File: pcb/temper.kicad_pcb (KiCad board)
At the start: 2 copper layers, 111.3 x 90 mm, 48 parts, among them J2 nice_view, SW1 SW_PUSH, SW10 SW_PUSH, SW11 SW_PUSH, SW12 SW_PUSH, SW13 SW_PUSH, SW14 SW_PUSH, SW15 SW_PUSH, SW16 SW_PUSH, SW17 SW_PUSH, SW18 SW_PUSH, SW2 SW_PUSH, SW3 SW_PUSH, SW4 SW_PUSH, SW5 SW_PUSH, SW6 SW_PUSH, SW7 SW_PUSH, SW8 SW_PUSH, SW9 SW_PUSH, U1 nice_nano

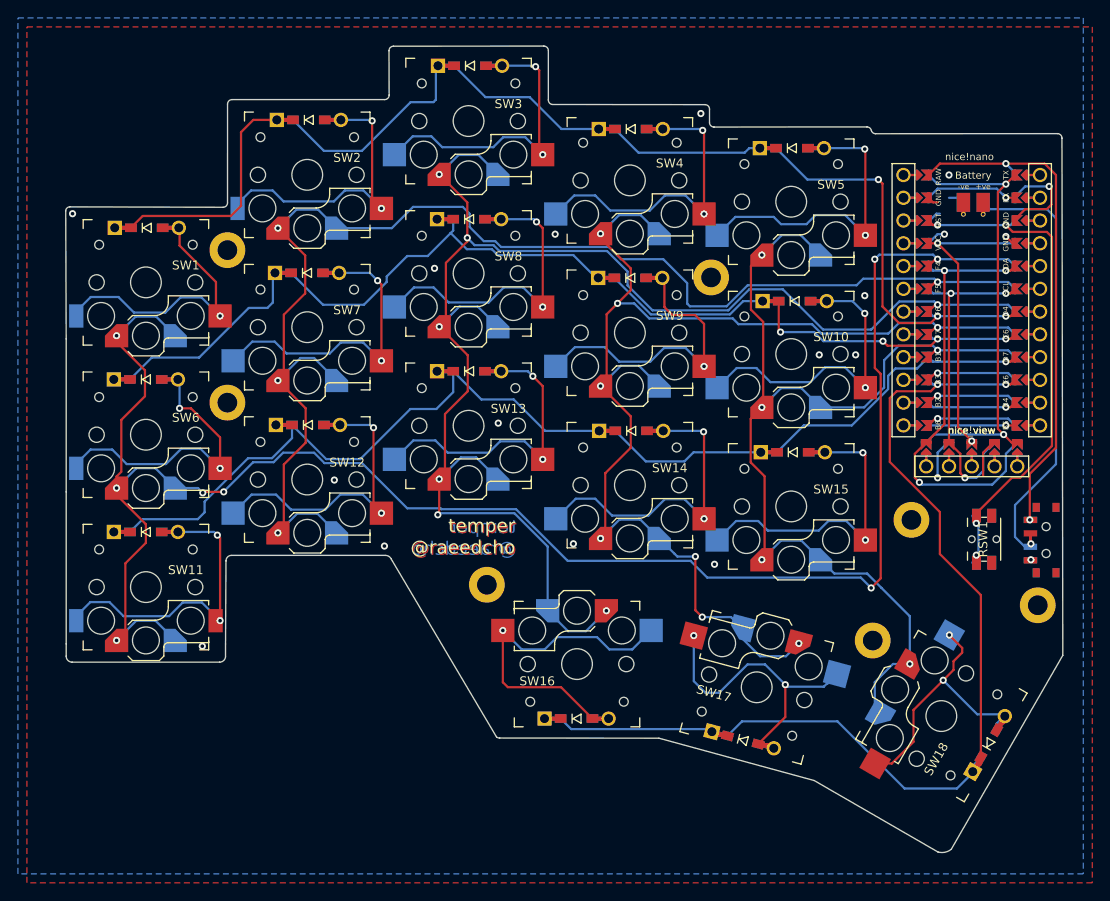
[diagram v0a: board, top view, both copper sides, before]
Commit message: Convert switches to Choc v2 sockets
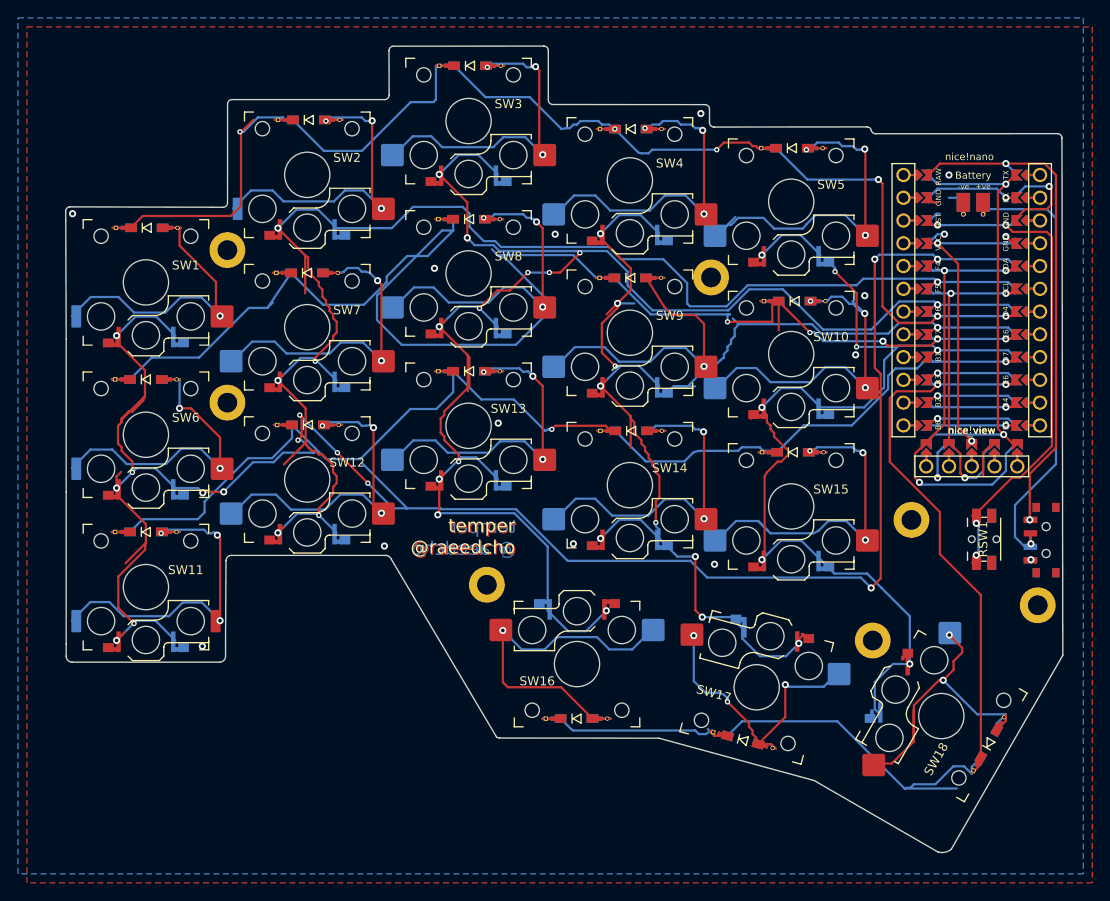
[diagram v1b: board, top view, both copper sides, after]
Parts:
- SW1, SW10, SW11, SW12, SW13, SW14, SW15, SW16, SW17, SW18, SW2, SW3, SW4, SW5, SW6, SW7, SW8, SW9: footprint dumta:Kailh_socket_PG1350_reversible -> dumta:Kailh_socket_Choc_V2_reversible
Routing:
- net row1: track 136.8 -> 186.3 mm, vias 4 -> 5
- net col0: track 205.5 -> 230.6 mm, vias 8 -> 14
- net col2: track 169.4 -> 187.2 mm, vias 7 -> 12
- net col3: track 138.5 -> 148.6 mm, vias 8 -> 10
- net col1: track 150.9 -> 159.6 mm, vias 4 -> 6
- net row3: track 122.1 -> 129.2 mm
- net Net-(D5-A): track 37.2 -> 43.6 mm, vias 2 -> 3
- net row0: track 150.3 -> 156.2 mm, vias 3 -> 6
- net row2: track 138.8 -> 143.7 mm, vias 1 -> 2
- net Net-(D15-A): track 37.2 -> 41.3 mm, vias 2 -> 3
- net Net-(D18-A): track 33.0 -> 36.8 mm
- net Net-(D4-A): track 37.4 -> 40.5 mm, vias 2 -> 3
- net Net-(D8-A): track 37.4 -> 40.2 mm, vias 2 -> 3
- net Net-(D12-A): track 37.3 -> 40.0 mm, vias 2 -> 3
- net Net-(D13-A): track 36.7 -> 39.4 mm, vias 2 -> 3
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
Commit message: Clean up Choc v2 manufacturing files
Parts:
- SW1: footprint dumta:Kailh_socket_Choc_V2_reversible -> dumta:Kailh_socket_Choc_V2_reversible_edge_left_SW1
- SW11: footprint dumta:Kailh_socket_Choc_V2_reversible -> dumta:Kailh_socket_Choc_V2_reversible_edge_both_SW11
- SW16: footprint dumta:Kailh_socket_Choc_V2_reversible -> dumta:Kailh_socket_Choc_V2_reversible_rot180_SW16
- SW17: footprint dumta:Kailh_socket_Choc_V2_reversible -> dumta:Kailh_socket_Choc_V2_reversible_rot165_SW17
- SW18: footprint dumta:Kailh_socket_Choc_V2_reversible -> dumta:Kailh_socket_Choc_V2_reversible_rot240_SW18
- SW2: footprint dumta:Kailh_socket_Choc_V2_reversible -> dumta:Kailh_socket_Choc_V2_reversible_edge_left_SW2
- SW6: footprint dumta:Kailh_socket_Choc_V2_reversible -> dumta:Kailh_socket_Choc_V2_reversible_edge_left_SW6
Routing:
- net col0: track 230.6 -> 216.8 mm
- net col3: track 148.6 -> 137.2 mm, vias 10 -> 9
- net col1: track 159.6 -> 150.0 mm
- net row1: track 186.3 -> 177.8 mm, vias 5 -> 10
- net row3: track 129.2 -> 121.3 mm, vias 2 -> 5
- net row0: track 156.2 -> 149.5 mm, vias 6 -> 10
- net col2: track 187.2 -> 181.2 mm
- net Net-(D5-A): track 43.6 -> 40.0 mm, vias 3 -> 4
- net row2: track 143.7 -> 140.1 mm, vias 2 -> 7
- net Net-(D10-A): track 37.0 -> 35.0 mm
- net Net-(D18-A): track 36.8 -> 36.0 mm, vias 2 -> 3
- net Net-(D1-A): track 35.5 -> 34.7 mm, vias 1 -> 2
- net Net-(D6-A): track 36.3 -> 35.6 mm, vias 2 -> 3
- net Net-(D9-A): track 37.4 -> 36.7 mm, vias 1 -> 2
- net Net-(D3-A): track 39.5 -> 38.7 mm, vias 3 -> 4
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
